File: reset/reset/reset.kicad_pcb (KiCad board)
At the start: 2 copper layers, 1 part

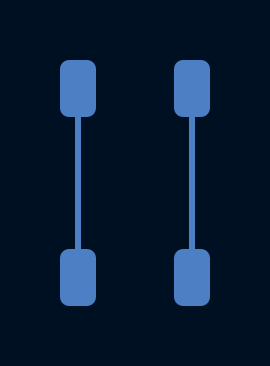
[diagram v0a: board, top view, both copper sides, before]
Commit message: update reset, remove led
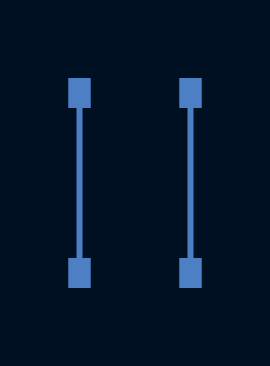
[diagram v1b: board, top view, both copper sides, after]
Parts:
- removed RESET_SW1: SW_Push, ErgoCai.pretty:K2-1187SQ
- added RESRT_SW1: TS-1187A-B-A-B, ErgoCai.pretty:SW-SMD_4P-L5.1-W5.1-P3.70-LS6.5-TL_H1.5, B.Cu at (0.00, 0.00)
